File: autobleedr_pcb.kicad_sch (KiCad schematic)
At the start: 20 parts, among them J11 Conn_01x02_Pin, J13 Screw_Terminal_01x08, J7 Screw_Terminal_01x02, Q1 PMOS, Q2 IRLML2060, SW1 SW_SPST, U2 ESP32, U6 TMC2209

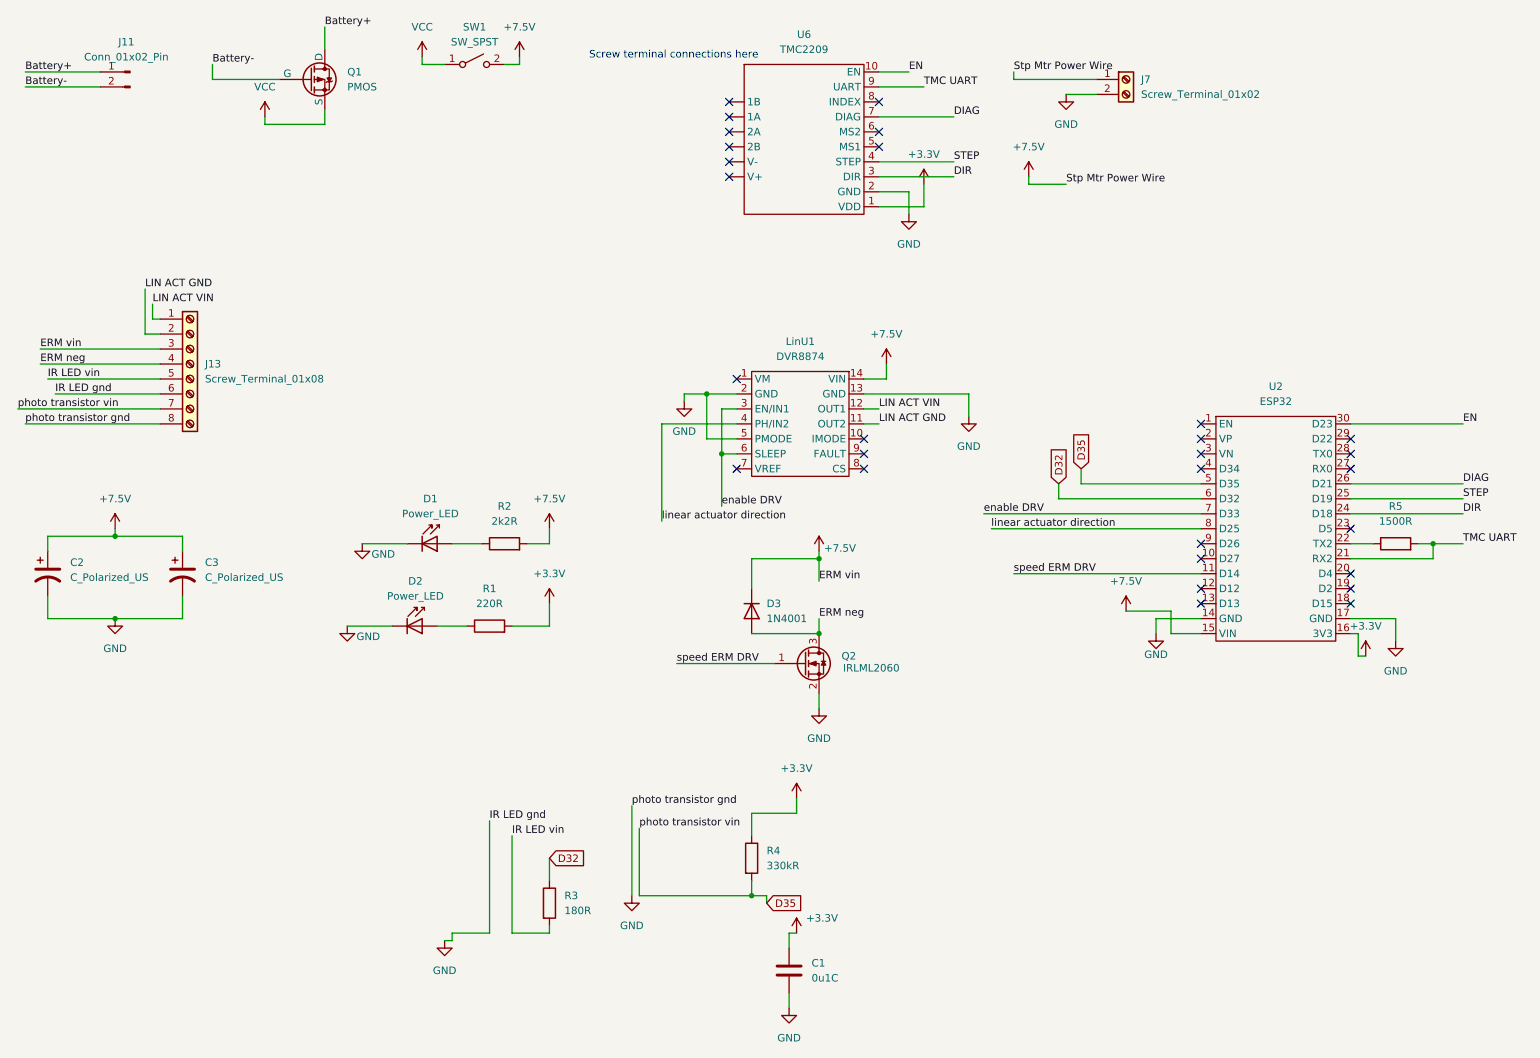
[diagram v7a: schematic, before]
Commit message: Added some silkscreen changes
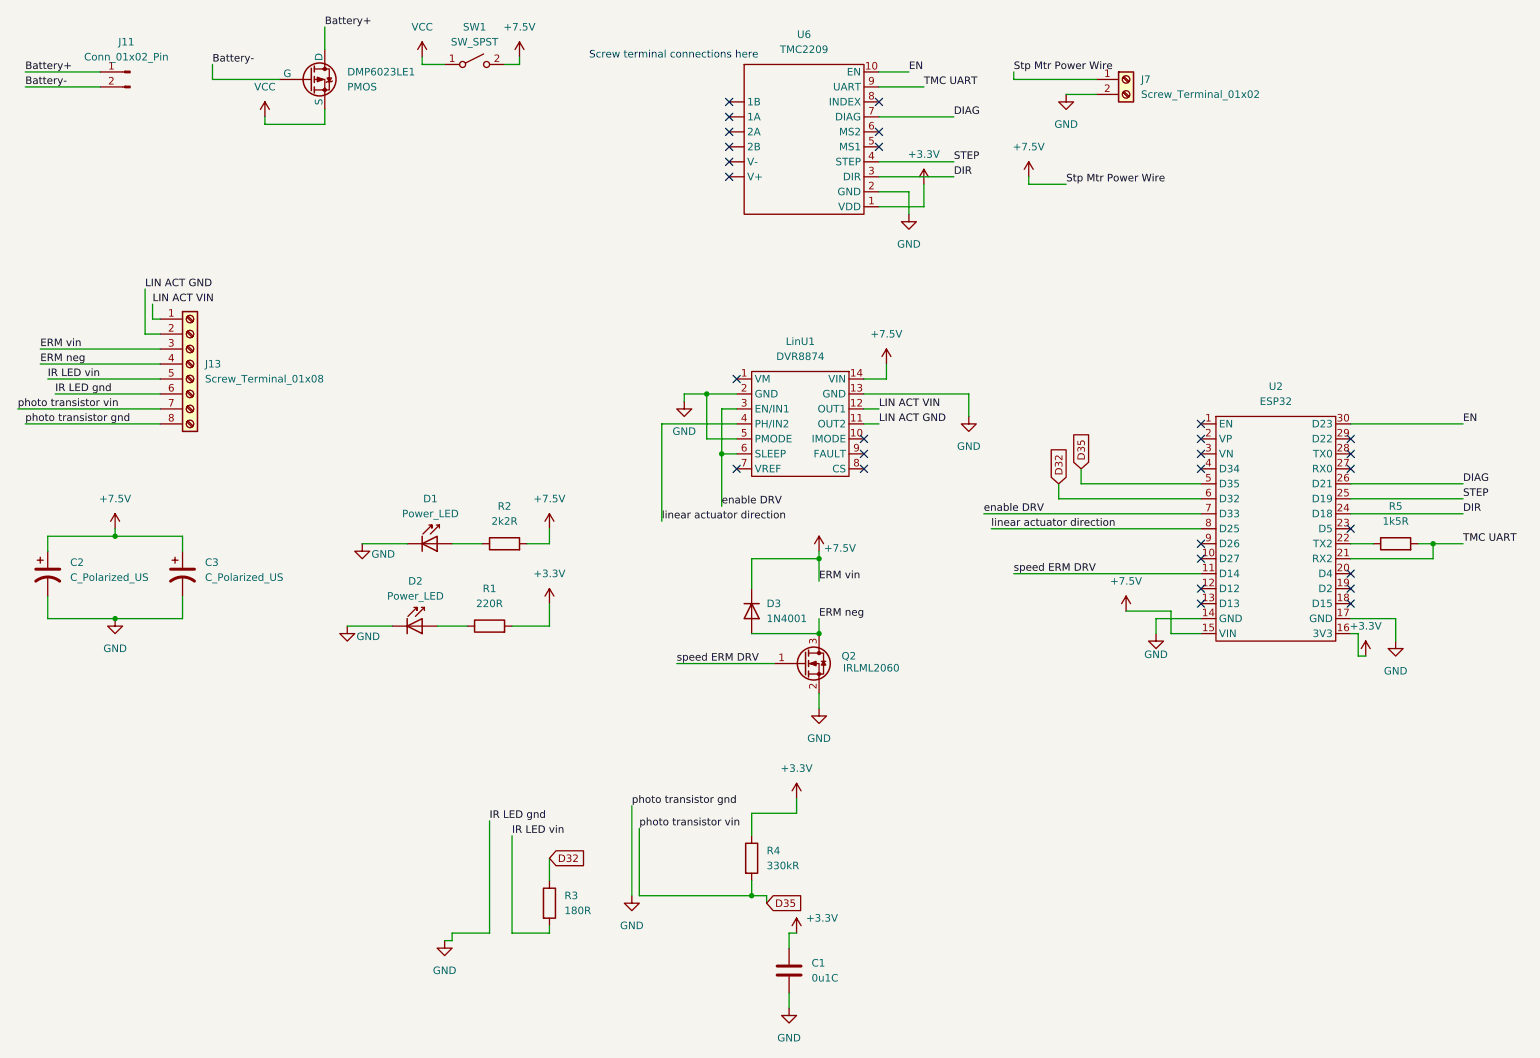
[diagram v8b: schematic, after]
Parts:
- R5: value 1500R -> 1k5R
- renumbered Q1 to DMP6023LE1
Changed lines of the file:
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@@
 			)
 		)
-		(property "Value" "1500R"
+		(property "Value" "1k5R"
 			(at 251.46 104.14 90)
 			(effects
@@
 		(dnp no)
 		(fields_autoplaced yes)
-		(property "Reference" "Q1"
+		(property "Reference" "DMP6023LE1"
 			(at 73.66 27.9399 0)
 			(effects
@@
 			(project ""
 				(path "/1cb070e6-4268-4590-be3a-70f1be021dfd"
-					(reference "Q1")
-					(unit 1)
-				)
+					(reference "DMP6023LE1")
+					(unit 1)
+				)
